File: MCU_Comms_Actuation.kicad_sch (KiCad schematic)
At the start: 26 parts, among them J1 MTSW-105-09-L-S-480, Y1 Crystal

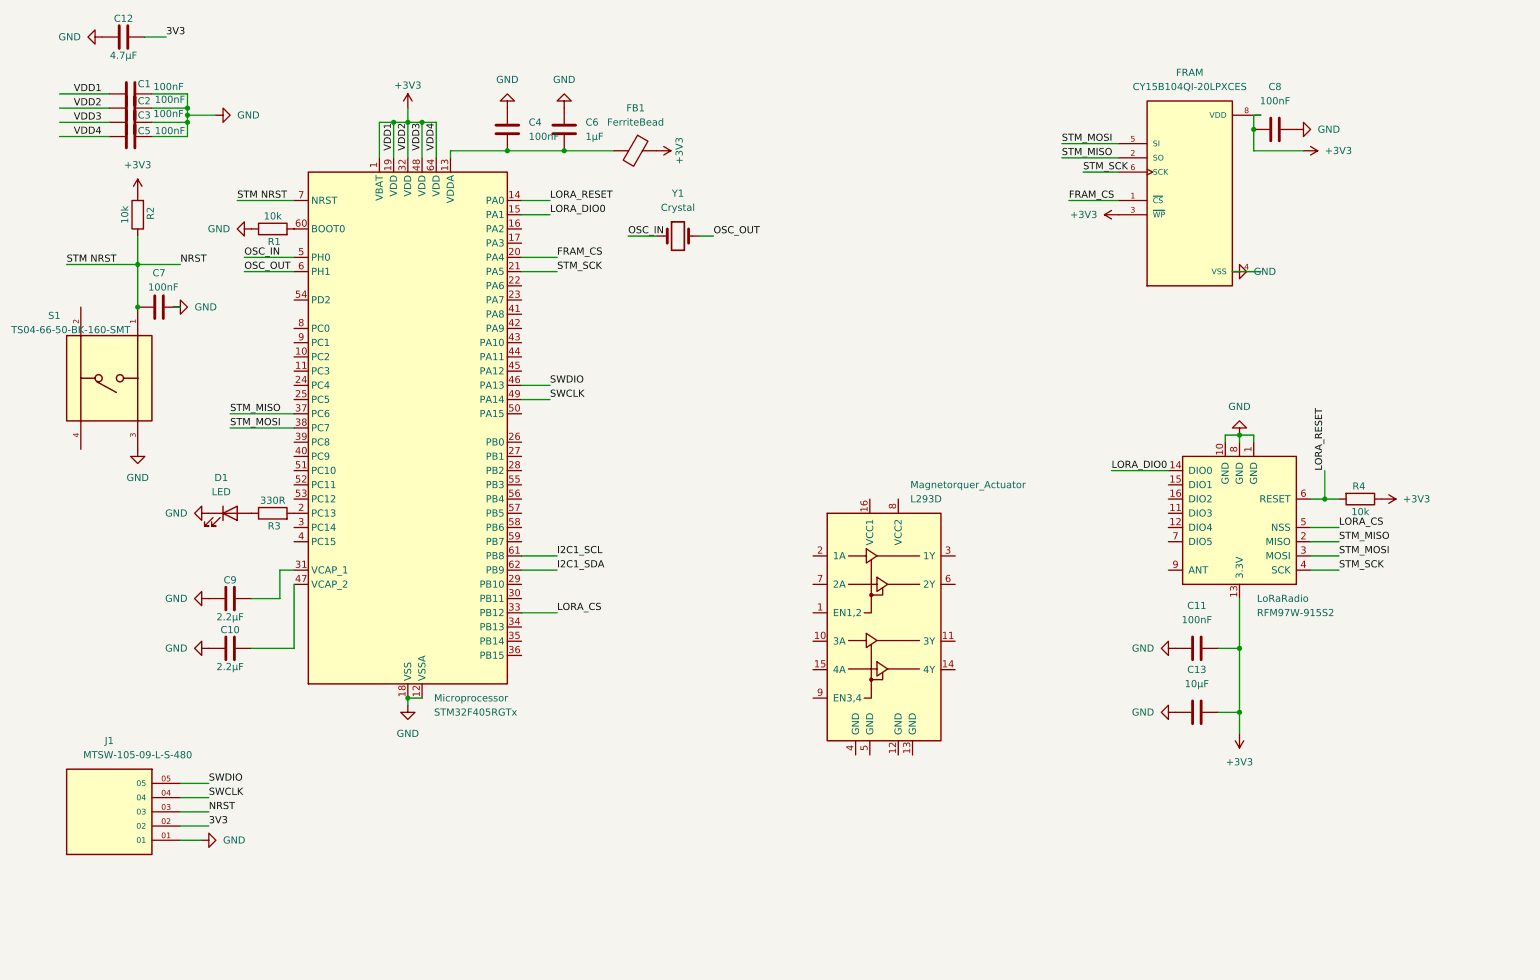
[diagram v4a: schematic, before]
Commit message: Add dual DRV8833 magnetorquer drivers with decoupling for XYZ axes
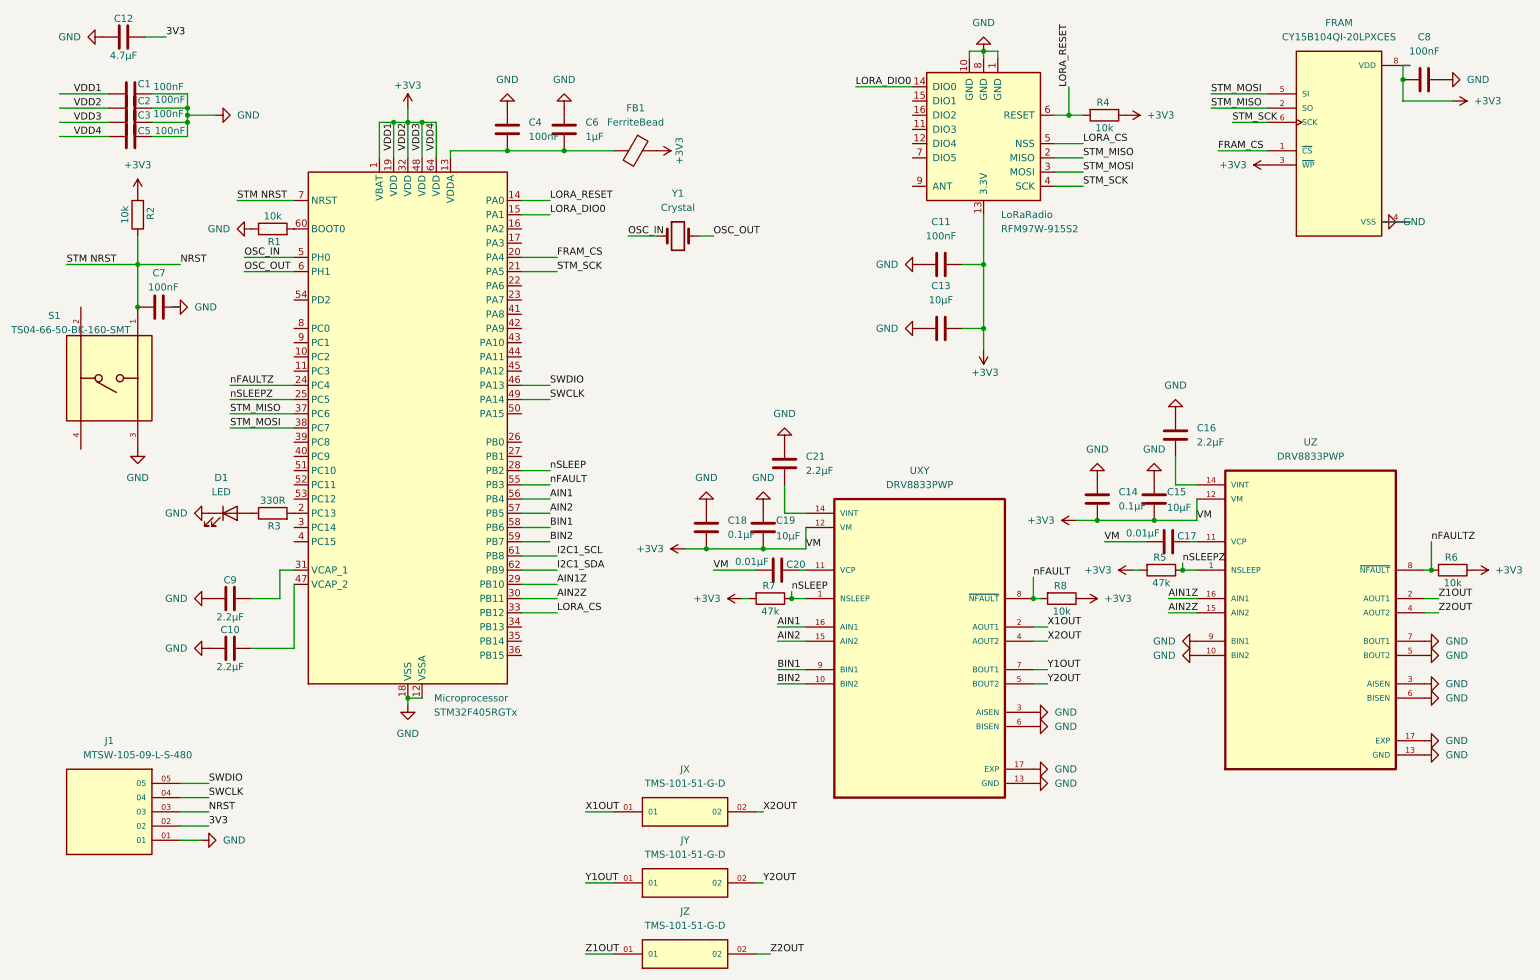
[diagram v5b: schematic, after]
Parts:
- removed Magnetorquer_Actuator: L293D, Package_DIP:DIP-16_W7.62mm, symbol Driver_Motor:L293D
- added C14, C18: 0.1µF, symbol Device:C
- added C15, C19: 10µF, symbol Device:C
- added C16, C21: 2.2µF, symbol Device:C
- added C17, C20: 0.01µF, symbol Device:C
- added JX, JY, JZ: TMS-101-51-G-D, TMS-101-51-G-D:SAMTEC_TMS-101-51-G-D, symbol TMS-101-51-G-D:TMS-101-51-G-D
- added R5, R7: 47k, symbol Device:R
- added R6, R8: 10k, symbol Device:R
- added UXY, UZ: DRV8833PWP, DRV8833PWP:IC_DRV8833PWP, symbol DRV8833PWP:DRV8833PWP
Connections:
- net +3V3: now also C14.2, C15.2, C17.2, C18.2, C19.2, C20.2, R5.2, R6.1, R7.2, R8.1, UXY.12 (VM), UZ.12 (VM)
- net GND: now also C14.1, C15.1, C16.1, C18.1, C19.1, C21.1, UXY.13 (GND), UXY.17 (EXP), UXY.3 (AISEN), UXY.6 (BISEN), UZ.10 (BIN2), UZ.13 (GND), UZ.17 (EXP), UZ.3 (AISEN), UZ.5 (BOUT2), UZ.6 (BISEN), UZ.7 (BOUT1), UZ.9 (BIN1)
- net nFAULTZ: now reaches Microprocessor.24 (PC4)
- net nFAULTZ: now also R6.2, UZ.8 (~{NFAULT})
- net nSLEEPZ: now reaches Microprocessor.25 (PC5)
- net nSLEEPZ: now also R5.1, UZ.1 (NSLEEP)
- net nSLEEP: now reaches Microprocessor.28 (PB2)
- net nSLEEP: now also R7.1, UXY.1 (NSLEEP)
- net AIN1Z: now reaches Microprocessor.29 (PB10)
- net AIN1Z: now also UZ.16 (AIN1)
- net AIN2Z: now reaches Microprocessor.30 (PB11)
- net AIN2Z: now also UZ.15 (AIN2)
- net nFAULT: now reaches Microprocessor.55 (PB3)
- net nFAULT: now also R8.2, UXY.8 (~{NFAULT})
- net AIN1: now reaches Microprocessor.56 (PB4)
- net AIN1: now also UXY.16 (AIN1)
- net AIN2: now reaches Microprocessor.57 (PB5)
- net AIN2: now also UXY.15 (AIN2)
- net BIN1: now reaches Microprocessor.58 (PB6)
- net BIN1: now also UXY.9 (BIN1)
- net BIN2: now reaches Microprocessor.59 (PB7)
- net BIN2: now also UXY.10 (BIN2)
- new net: C20.1, UXY.11 (VCP)
- new net: C21.2, UXY.14 (VINT)
- new net: C16.2, UZ.14 (VINT)
- new net: C17.1, UZ.11 (VCP)
- new net X1OUT: JX.01, UXY.2 (AOUT1)
- new net X2OUT: JX.02, UXY.4 (AOUT2)
- new net Y1OUT: JY.01, UXY.7 (BOUT1)
- new net Y2OUT: JY.02, UXY.5 (BOUT2)
- new net Z1OUT: JZ.01, UZ.2 (AOUT1)
- new net Z2OUT: JZ.02, UZ.4 (AOUT2)
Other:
- moved on the sheet: C11, C13, C8, FRAM, LoRaRadio, R4

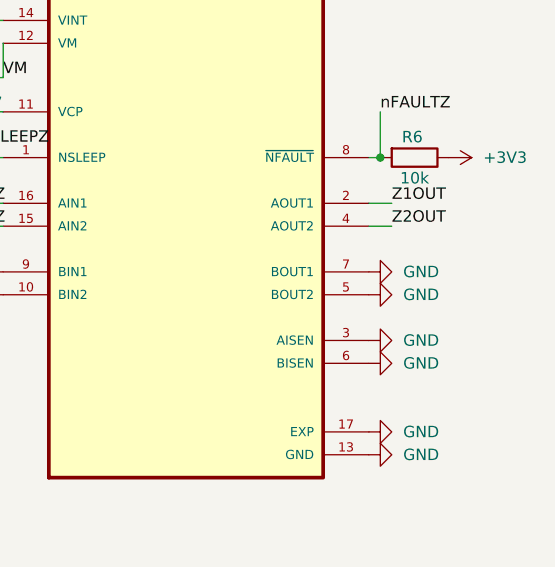
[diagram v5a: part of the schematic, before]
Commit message: Fix C15 cap value and add NC markers on unused BOUT pins
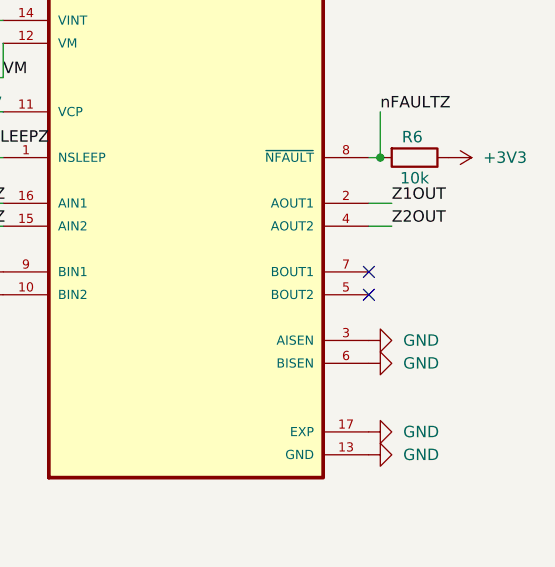
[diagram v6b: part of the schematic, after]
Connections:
- net GND: no longer UZ.5 (BOUT2), UZ.7 (BOUT1)
- no-connect marks 0 -> 2
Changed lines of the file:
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@@
 		(color 0 0 0 0)
 	)
+	(no_connect
+		(at 265.43 134.62)
+	)
+	(no_connect
+		(at 265.43 132.08)
+	)
 	(wire
 		(pts
@@
 	)
 	(symbol
-		(lib_id "power:GND")
-		(at 265.43 134.62 90)
-		(unit 1)
-		(body_style 1)
-		(exclude_from_sim no)
-		(in_bom yes)
-		(on_board yes)
-		(in_pos_files yes)
-		(dnp no)
-		(fields_autoplaced yes)
-		(property "Reference" "#PWR048"
-			(at 271.78 134.62 0)
-			(hide yes)
-			(show_name no)
-			(do_not_autoplace no)
-			(effects
-				(font
-					(size 1.27 1.27)
-				)
-			)
-		)
-		(property "Value" "GND"
-			(at 269.24 134.6199 90)
-			(show_name no)
-			(do_not_autoplace no)
-			(effects
-				(font
-					(size 1.27 1.27)
-				)
-				(justify right)
-			)
-		)
-		(property "Footprint" ""
-			(at 265.43 134.62 0)
-			(hide yes)
-			(show_name no)
-			(do_not_autoplace no)
-			(effects
-				(font
-					(size 1.27 1.27)
-				)
-			)
-		)
-		(property "Datasheet" ""
-			(at 265.43 134.62 0)
-			(hide yes)
-			(show_name no)
-			(do_not_autoplace no)
-			(effects
-				(font
-					(size 1.27 1.27)
-				)
-			)
-		)
-		(property "Description" "Power symbol creates a global label with name \"GND\" , ground"
-			(at 265.43 134.62 0)
-			(hide yes)
-			(show_name no)
-			(do_not_autoplace no)
-			(effects
-				(font
-					(size 1.27 1.27)
-				)
-			)
-		)
-		(pin "1"
-		)
-		(instances
-			(project "MCU_Comms_Actuation"
-				(path "/951c21f5-e3a2-4971-b4ad-b39d9271a0ce"
-					(reference "#PWR048")
-					(unit 1)
-				)
-			)
-		)
-	)
-	(symbol
 		(lib_id "Device:C")
 		(at 207.01 106.68 0)
@@
 					(unit 1)
 				)
-			)
-		)
-	)
-	(symbol
-		(lib_id "power:GND")
-		(at 265.43 132.08 90)
-		(unit 1)
-		(body_style 1)
-		(exclude_from_sim no)
-		(in_bom yes)
-		(on_board yes)
-		(in_pos_files yes)
-		(dnp no)
-		(fields_autoplaced yes)
-		(property "Reference" "#PWR047"
-			(at 271.78 132.08 0)
-			(hide yes)
-			(show_name no)
-			(do_not_autoplace no)
-			(effects
-				(font
-					(size 1.27 1.27)
-				)
-			)
-		)
-		(property "Value" "GND"
-			(at 269.24 132.0799 90)
-			(show_name no)
-			(do_not_autoplace no)
-			(effects
-				(font
-					(size 1.27 1.27)
-				)
-				(justify right)
-			)
-		)
-		(property "Footprint" ""
-			(at 265.43 132.08 0)
-			(hide yes)
-			(show_name no)
-			(do_not_autoplace no)
-			(effects
-				(font
-					(size 1.27 1.27)
-				)
-			)
-		)
-		(property "Datasheet" ""
-			(at 265.43 132.08 0)
-			(hide yes)
-			(show_name no)
-			(do_not_autoplace no)
-			(effects
-				(font
-					(size 1.27 1.27)
-				)
-			)
-		)
-		(property "Description" "Power symbol creates a global label with name \"GND\" , ground"
-			(at 265.43 132.08 0)
-			(hide yes)
-			(show_name no)
-			(do_not_autoplace no)
-			(effects
-				(font
-					(size 1.27 1.27)
-				)
-			)
-		)
-		(pin "1"
-		)
-		(instances
-			(project "MCU_Comms_Actuation"
-				(path "/951c21f5-e3a2-4971-b4ad-b39d9271a0ce"
-					(reference "#PWR047")
-					(unit 1)
-				)
